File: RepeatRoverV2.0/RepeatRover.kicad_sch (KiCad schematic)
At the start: 10 parts

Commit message: updated mcu
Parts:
- added C11, C12: 12pF, Capacitor_SMD:C_0805_2012Metric, symbol Device:C
- added C4: 100nF, Capacitor_SMD:C_0805_2012Metric, symbol Device:C
- added SB1, SB2, SB3, SB4: SolderJumper_2_Bridged, symbol Jumper:SolderJumper_2_Bridged
- added TP1, TP2: TestPoint, symbol Connector:TestPoint
- added X2: 32.768kHz, symbol Device:Crystal
- C1: value (none) -> 1uF; footprint (none) -> Capacitor_SMD:C_0805_2012Metric
- C2: value (none) -> 10uF; footprint (none) -> Capacitor_SMD:C_0805_2012Metric
- MAG: value (none) -> MMC5983MA; footprint (none) -> MMC5983MA:PQFN50P300X300X100-16N
- MCU: value (none) -> NRF52832-QFAA-R; footprint (none) -> NRF52832-QFAA-R:QFN40P600X600X90-49N
- SD_SLOT: value (none) -> 104031-0811; footprint (none) -> 104031-0811:MOLEX_104031-0811
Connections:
- net GND: now also C11.1, C12.1, C4.1
- net at MCU.1 (DEC1): now also C4.2
- net at MCU.2 (P0.00): now also SB2.1 (A), SB4.2 (B)
- net at MCU.3 (P0.01): now also SB1.1 (A), SB3.2 (B)
- new net: SB4.1 (A), TP1.1
- new net: C12.2, SB1.2 (B), X2.1
- new net: C11.2, SB2.2 (B), X2.2
- new net: SB3.1 (A), TP2.1
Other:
- moved on the sheet: C1, C2, C3, C4, MCU, h-bridge

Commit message: V3 W/ Partial PCB Design
Added new H-Bridge Symbol, Mapped NRF required components, finished breakout board for MMC
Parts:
- removed C11, C12: 12pF, Capacitor_SMD:C_0805_2012Metric, symbol Device:C
- removed C4: 100nF, Capacitor_SMD:C_0805_2012Metric, symbol Device:C
- removed SB1, SB2, SB3, SB4: SolderJumper_2_Bridged, symbol Jumper:SolderJumper_2_Bridged
- removed TP1, TP2: TestPoint, symbol Connector:TestPoint
- removed X2: 32.768kHz, symbol Device:Crystal
- C1: value 1uF -> (none); footprint Capacitor_SMD:C_0805_2012Metric -> (none)
- C2: value 10uF -> (none); footprint Capacitor_SMD:C_0805_2012Metric -> (none)
- MAG: value MMC5983MA -> (none); footprint MMC5983MA:PQFN50P300X300X100-16N -> (none)
- MCU: value NRF52832-QFAA-R -> (none); footprint NRF52832-QFAA-R:QFN40P600X600X90-49N -> (none)
- SD_SLOT: value 104031-0811 -> (none); footprint 104031-0811:MOLEX_104031-0811 -> (none)
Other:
- moved on the sheet: C1, C2, C3, C4, MCU, h-bridge

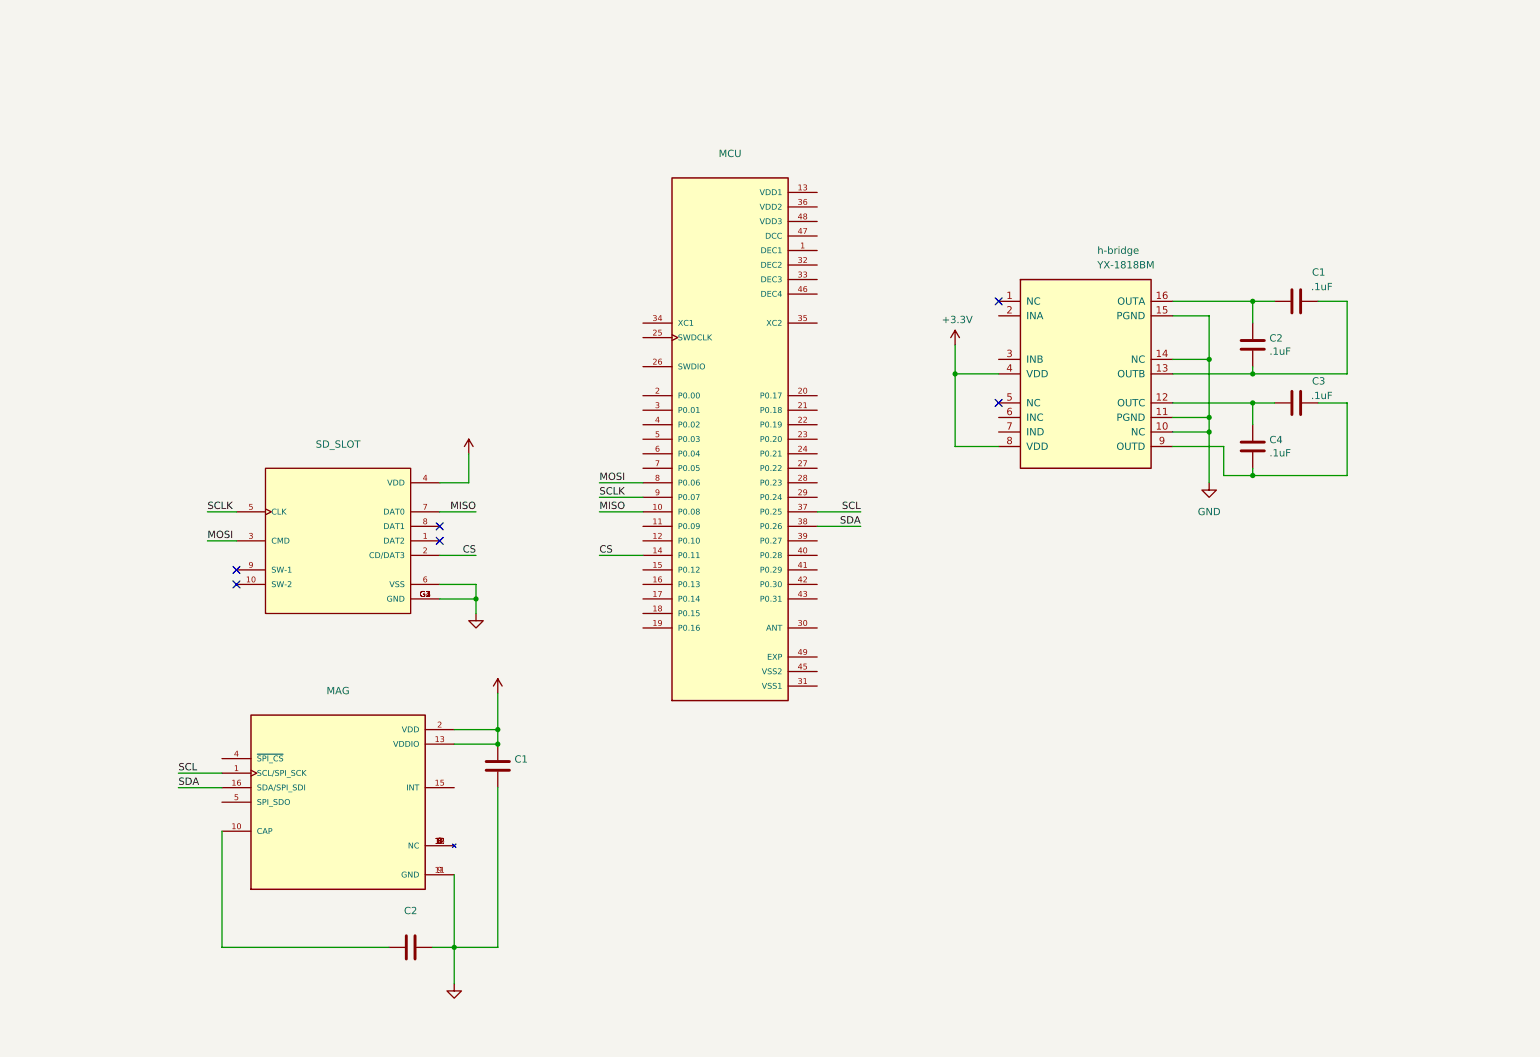
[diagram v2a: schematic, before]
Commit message: new mcu footgprint
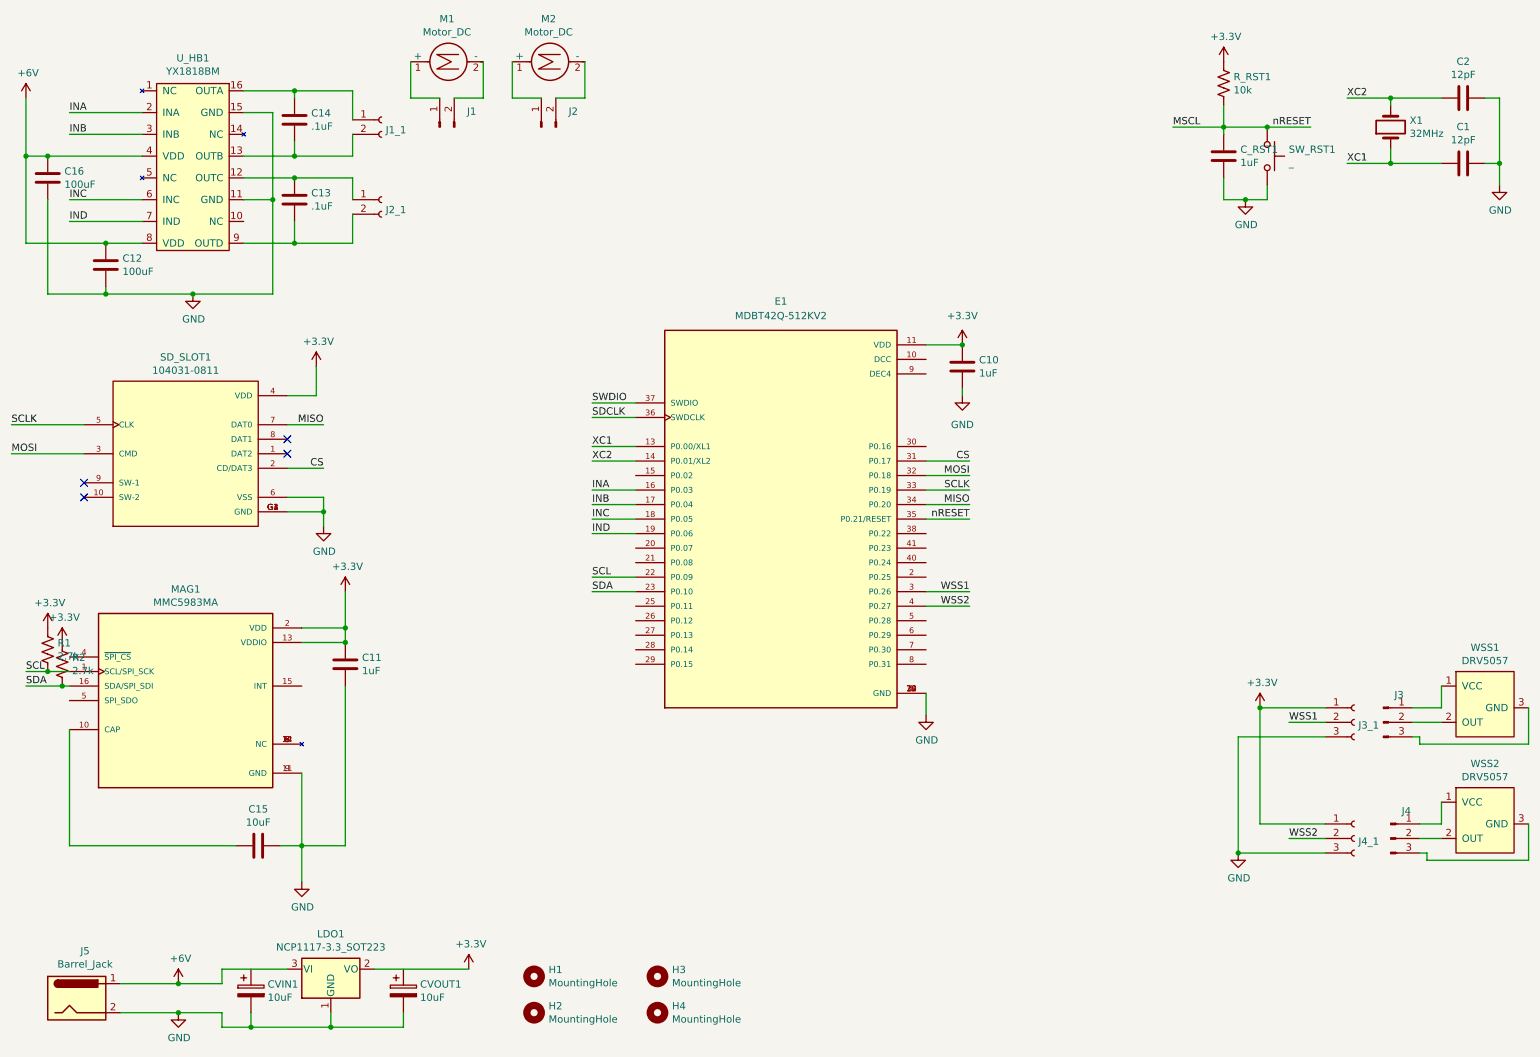
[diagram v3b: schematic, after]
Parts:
- removed C3, C4: .1uF, Capacitor_SMD:C_0805_2012Metric, symbol Device:C
- removed MCU: (no value), symbol NRF52832-QFAA-R:NRF52832-QFAA-R
- removed h-bridge: YX-1818BM, symbol Interface_Expansion:PCA9516
- added C10, C_RST1: 1uF, Capacitor_SMD:C_0805_2012Metric_Pad1.18x1.45mm_HandSolder, symbol Device:C
- added C12, C16: 100uF, Capacitor_SMD:C_0805_2012Metric_Pad1.18x1.45mm_HandSolder, symbol Device:C
- added C13, C14: .1uF, Capacitor_SMD:C_0805_2012Metric_Pad1.18x1.45mm_HandSolder, symbol Device:C
- added CVIN1, CVOUT1: 10uF, Capacitor_SMD:CP_Elec_5x5.7, symbol Device:C_Polarized
- added E1: MDBT42Q-512KV2, symbol MDBT42Q-512KV2:MDBT42Q-512KV2
- added H1, H2, H3, H4: MountingHole, MountingHole:MountingHole_3.2mm_M3, symbol Mechanical:MountingHole
- added J1, J2: Conn_01x02_Male, symbol Connector:Conn_01x02_Male
- added J1_1, J2_1: Conn_01x02_Female, Connector_PinSocket_2.54mm:PinSocket_1x02_P2.54mm_Vertical, symbol Connector:Conn_01x02_Female
- added J3, J4: Conn_01x03_Male, symbol Connector:Conn_01x03_Male
- added J3_1, J4_1: Conn_01x03_Female, Connector_PinSocket_2.54mm:PinSocket_1x03_P2.54mm_Vertical, symbol Connector:Conn_01x03_Female
- added J5: Barrel_Jack, Connector_BarrelJack:BarrelJack_CUI_PJ-102AH_Horizontal, symbol Connector:Barrel_Jack
- added LDO1: NCP1117-3.3_SOT223, Package_TO_SOT_SMD:SOT-223-3_TabPin2, symbol Regulator_Linear:NCP1117-3.3_SOT223
- added M1, M2: Motor_DC, symbol Motor:Motor_DC
- added R1, R2: 2.7k, Resistor_SMD:R_0805_2012Metric_Pad1.20x1.40mm_HandSolder, symbol Device:R_US
- added R_RST1: 10k, Resistor_SMD:R_0805_2012Metric_Pad1.20x1.40mm_HandSolder, symbol Device:R_US
- added SW_RST1: _, Button_Switch_THT:SW_PUSH_6mm, symbol Switch:SW_Push
- added U_HB1: YX1818BM, Package_SO:SOP-16_4.55x10.3mm_P1.27mm, symbol HallEffect:YX1818BM
- added WSS1, WSS2: DRV5057, symbol HallEffect:DRV5057
- added X1: 32MHz, Hall Effect Footprint:OSC_XRCGB32M000FXH2CR0, symbol Device:Crystal
- C1, C2: value .1uF -> 12pF; footprint Capacitor_SMD:C_0805_2012Metric -> Capacitor_SMD:C_0805_2012Metric_Pad1.18x1.45mm_HandSolder
- C11: renamed from C1; value (none) -> 1uF; footprint (none) -> Capacitor_SMD:C_0805_2012Metric_Pad1.18x1.45mm_HandSolder
- C15: renamed from C2; value (none) -> 10uF; footprint (none) -> Capacitor_SMD:C_0805_2012Metric_Pad1.18x1.45mm_HandSolder
- MAG1: renamed from MAG; value (none) -> MMC5983MA; footprint (none) -> MMC5983MA:PQFN50P300X300X100-16N
- SD_SLOT1: renamed from SD_SLOT; value (none) -> 104031-0811; footprint (none) -> 104031-0811:MOLEX_104031-0811
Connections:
- net +3V0 is gone; now on net +3V3: C11.2, MAG1.13 (VDDIO), MAG1.2 (VDD)
- net +3V3: now also C10.1, E1.11 (VDD), J3_1.1 (Pin_1), J4_1.1 (Pin_1), LDO1.2 (VO), R1.1, R2.1, R_RST1.1
- net CS: now also E1.31 (P0.17)
- net GND: now also C1.2, C2.2, C10.2, C12.1, C16.1, CVIN1.2, CVOUT1.2, C_RST1.2, E1.1 (GND), E1.12 (GND), E1.24 (GND), E1.39 (GND), J3_1.3 (Pin_3), J4_1.3 (Pin_3), J5.2, LDO1.1 (GND), SW_RST1.2, U_HB1.11 (GND), U_HB1.15 (GND)
- net MISO: now also E1.34 (P0.20)
- net MOSI: now also E1.32 (P0.18)
- net SCL: now also E1.22 (P0.09), R1.2
- net SCLK: now also E1.33 (P0.19)
- net SDA: now also E1.23 (P0.10), R2.2
- net XC1: now reaches C1.1
- net XC1: now also E1.13 (P0.00/XL1), X1.1; no longer C2.1
- new net: J3.1 (Pin_1), WSS1.1 (VCC)
- new net: J3.2 (Pin_2), WSS1.2 (OUT)
- new net: J3.3 (Pin_3), WSS1.3 (GND)
- new net: J4.1 (Pin_1), WSS2.1 (VCC)
- new net: J4.2 (Pin_2), WSS2.2 (OUT)
- new net: J4.3 (Pin_3), WSS2.3 (GND)
- new net: C13.2, J2_1.1 (Pin_1), U_HB1.12 (OUTC)
- new net: C14.1, J1_1.2 (Pin_2), U_HB1.13 (OUTB)
- new net: C14.2, J1_1.1 (Pin_1), U_HB1.16 (OUTA)
- new net: C13.1, J2_1.2 (Pin_2), U_HB1.9 (OUTD)
- new net: J1.1 (Pin_1), M1.1 (+)
- new net: J1.2 (Pin_2), M1.2 (-)
- new net: J2.1 (Pin_1), M2.1 (+)
- new net: J2.2 (Pin_2), M2.2 (-)
- new net +6V: C12.2, C16.2, J5.1, LDO1.3 (VI), U_HB1.4 (VDD), U_HB1.8 (VDD)
- new net INA: E1.16 (P0.03), U_HB1.2 (INA)
- new net INB: E1.17 (P0.04), U_HB1.3 (INB)
- new net INC: E1.18 (P0.05), U_HB1.6 (INC)
- new net IND: E1.19 (P0.06), U_HB1.7 (IND)
- new net MSCL: C_RST1.1, E1.35 (P0.21/RESET), R_RST1.2, SW_RST1.1
- new net SDCLK: E1.36 (SWDCLK)
- new net SWDIO: E1.37 (SWDIO)
- new net WSS1: E1.3 (P0.26), J3_1.2 (Pin_2)
- new net WSS2: E1.4 (P0.27), J4_1.2 (Pin_2)
- new net XC2: C2.1, E1.14 (P0.01/XL2), X1.2
- no-connect marks 6 -> 4
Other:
- moved on the sheet: C11, C15, MAG1, SD_SLOT1
